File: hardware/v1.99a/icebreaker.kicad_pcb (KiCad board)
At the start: 4 copper layers, 50 x 37 mm, 125 parts, among them J1 USB_C_Receptacle_USB2.0, J14 Jumper, J19 Jumper, J2 Conn_02x05_Odd_Even, J20 Flash, J21 PMOD, J22 PMOD, J23 PMOD, J26 5V AUX, J27 5V AUX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

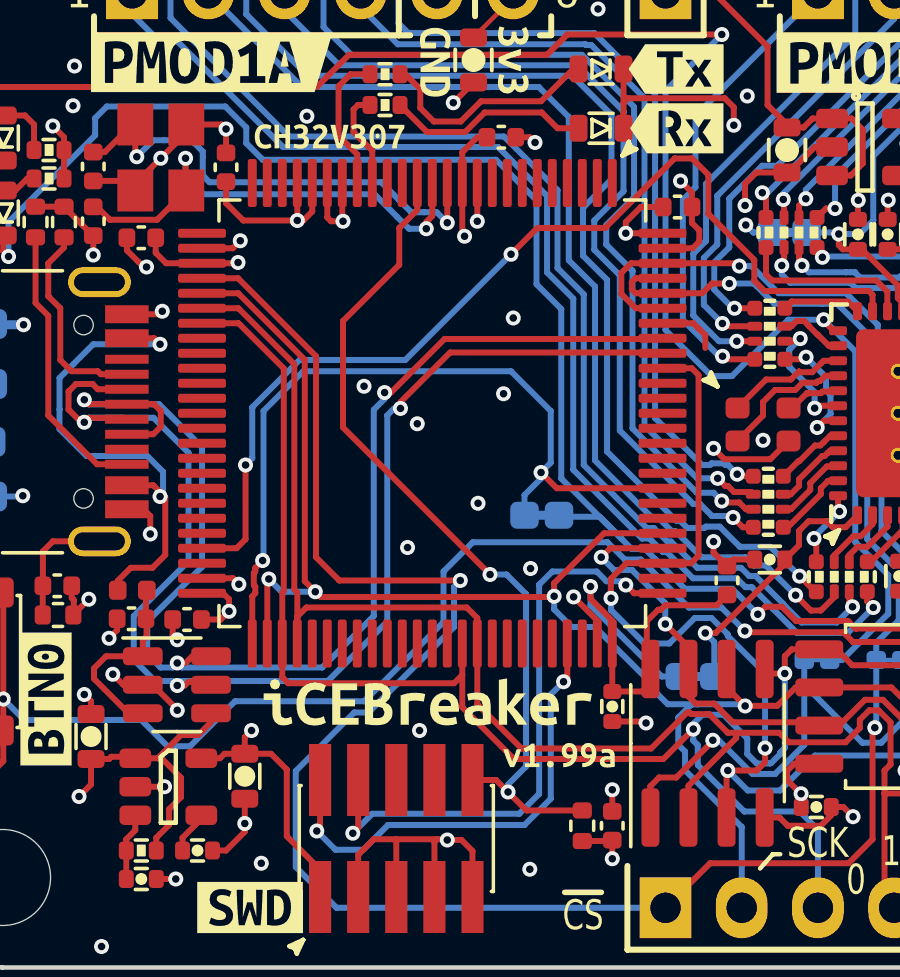
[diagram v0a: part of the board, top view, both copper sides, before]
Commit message: v1.99a: Move FGPA_CLK to MCO pin.
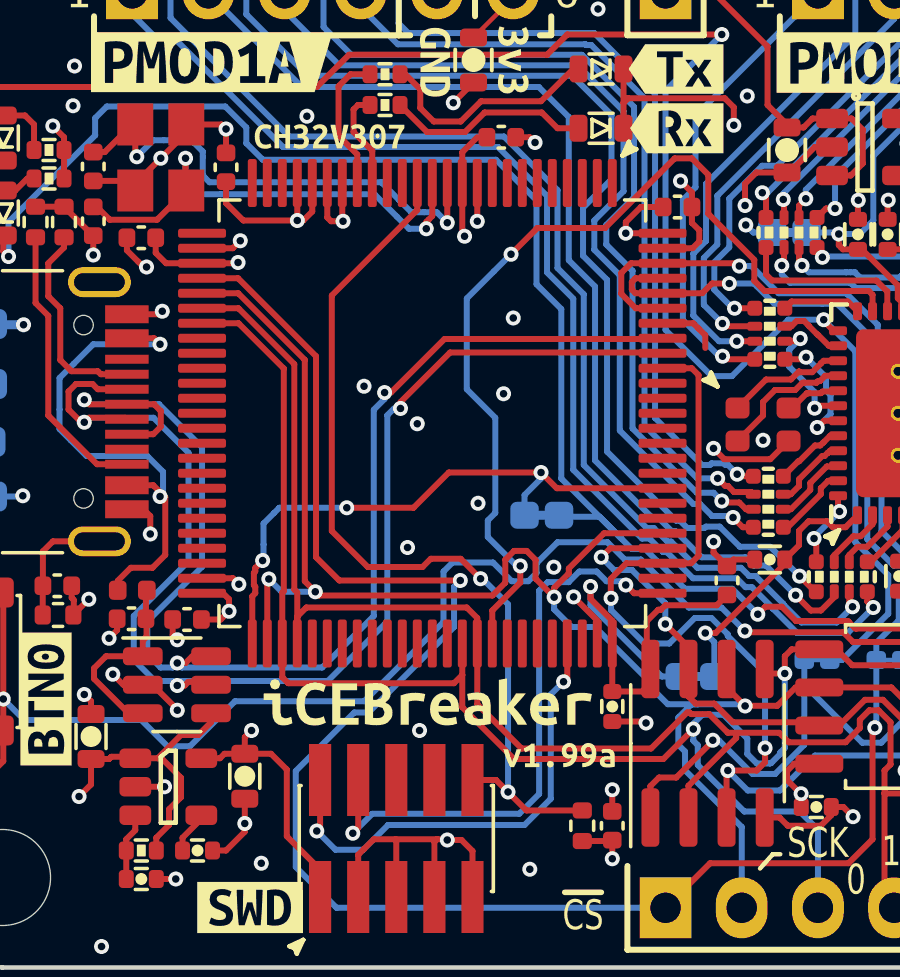
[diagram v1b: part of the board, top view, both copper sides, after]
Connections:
- U4 pad 47: FTDI_CLK -> unconnected-(U4-Pad47)
- U4 pad 67: unconnected-(U4-Pad67) -> FTDI_CLK
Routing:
- net iCE_CS: track 26.7 -> 20.1 mm, vias 2 -> 3
- net iCE_SCK: track 69.7 -> 71.8 mm
- net FTDI_CLK: track 33.8 -> 32.0 mm
- net /usb-if/NRST: track 28.5 -> 30.2 mm
- net /~{BUTTON}: track 51.6 -> 52.4 mm

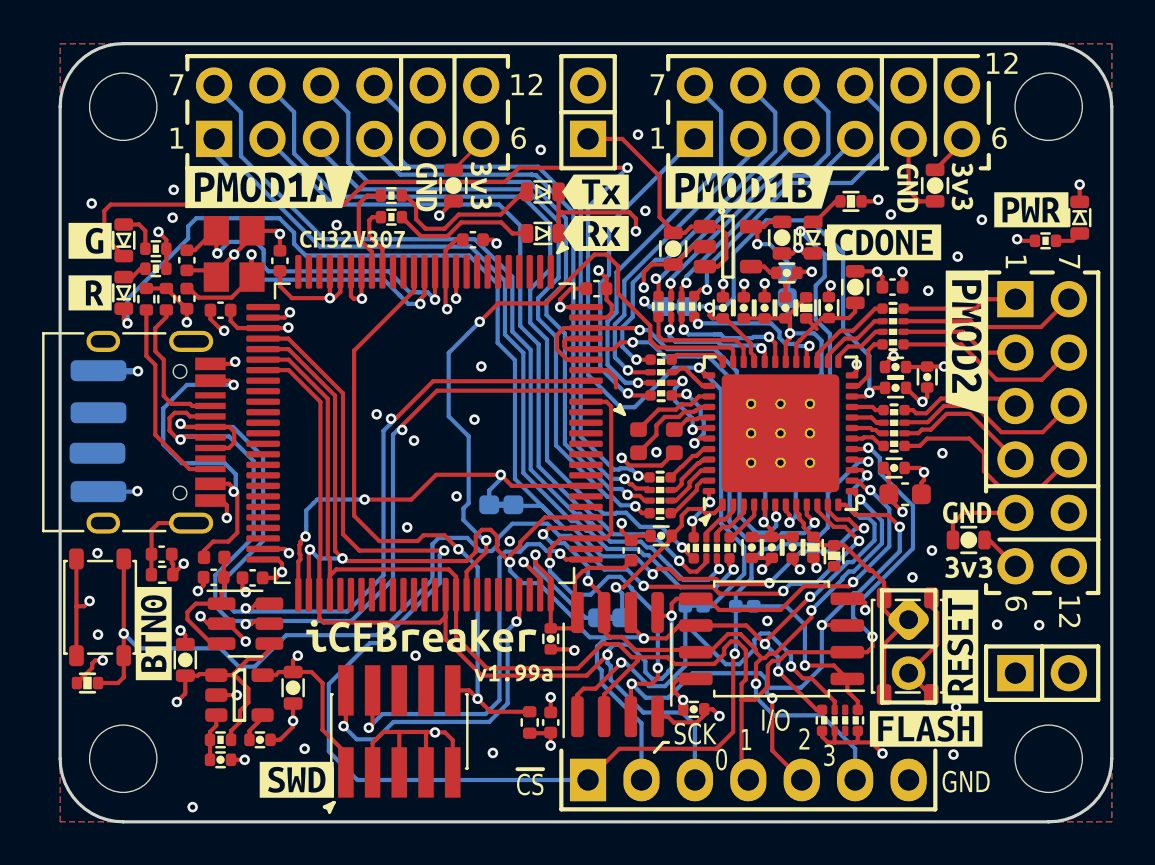
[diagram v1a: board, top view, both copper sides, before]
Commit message: v1.99a: Update
- Rename nets
- Add Debug UART channel to 10P SWD connector
- Add analog mux default on for iCE_CS/FLASH_CS
- Connect DONE/RESET
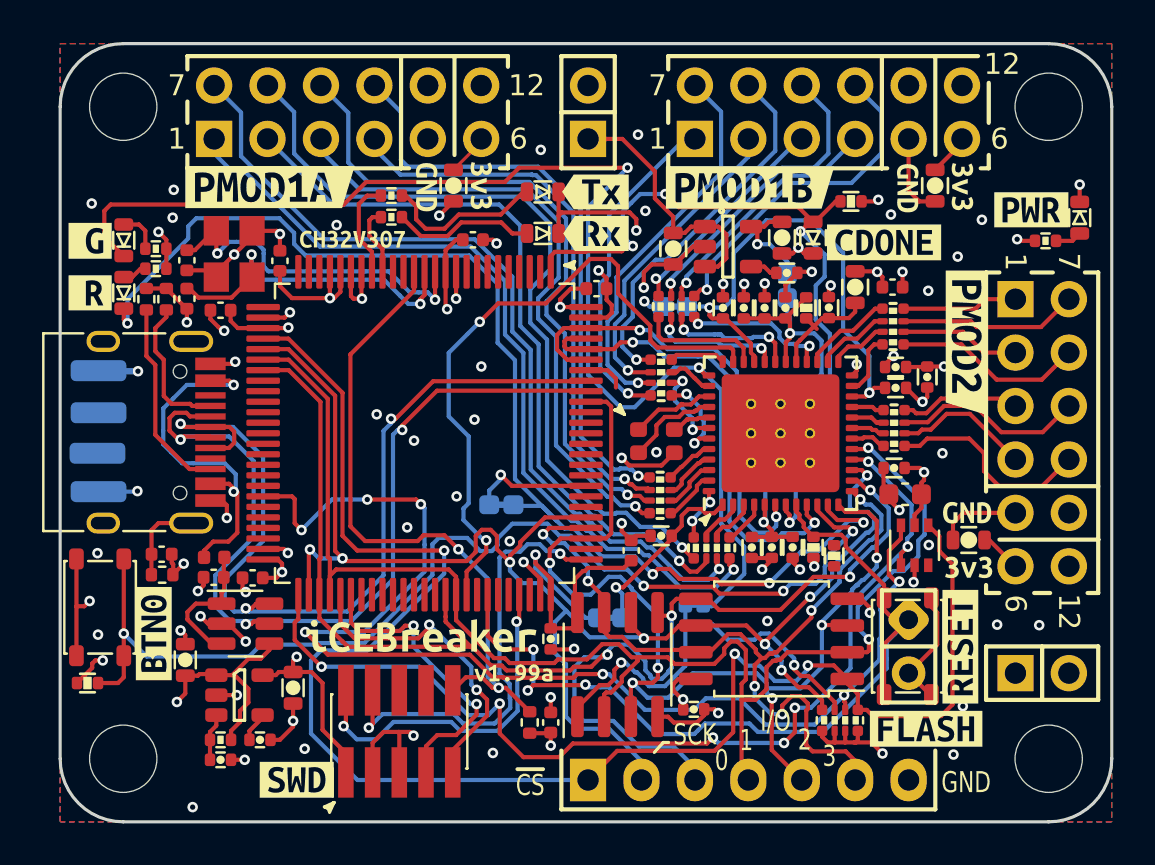
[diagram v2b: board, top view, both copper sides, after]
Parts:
- removed JP2: Flash_CS-SPI_CS, pkl_jumpers:J_NC_0402_15
- added U8: 74LVC1G3157, Package_TO_SOT_SMD:SOT-363_SC-70-6, F.Cu at (70.6, 52.9)
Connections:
- net FLASH_MISO|IO1 renamed FLASH_CIPO|IO1
- net FLASH_MOSI|IO0 renamed FLASH_COPI|IO0
- D3 pad A: /iCE_CDONE -> iCE_CDONE
- J2 pad 7: GND -> /usb-if/DEBUG_RXD
- J2 pad 9: GND -> /usb-if/DEBUG_TXD
- J28 pad 1: /iCE_CRESET -> iCE_CRESET
- J3 pad 2: iCE_CS -> iCE_USER_CS
- R12 pad 2: /iCE_CDONE -> iCE_CDONE
- R19 pad 2: /iCE_CRESET -> iCE_CRESET
- R7 pad 5: (no net) -> +3V3
- R7 pad 6: (no net) -> iCE_CS_SEL
- R7 pad 8: /FLASH_~{CS} -> FLASH_CS
- SW2 pad 1: /iCE_CRESET -> iCE_CRESET
- U4 pad 1: unconnected-(U4-Pad1) -> iCE_CDONE
- U4 pad 44: unconnected-(U4-Pad44) -> iCE_CS_SEL
- U4 pad 55: unconnected-(U4-Pad55) -> /usb-if/DEBUG_TXD
- U4 pad 56: unconnected-(U4-Pad56) -> /usb-if/DEBUG_RXD
- U4 pad 69: unconnected-(U4-Pad69) -> iCE_CRESET
- U4 pad 83: iCE_CS -> iCE_USER_CS
- U6 pad 16: FLASH_CS -> iCE_CS
- U6 pad 35: FTDI_CLK -> FPGA_CLK
- U6 pad 7: /iCE_CDONE -> iCE_CDONE
- U6 pad 8: /iCE_CRESET -> iCE_CRESET
- U7 pad 1: /FLASH_~{CS} -> FLASH_CS
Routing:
- net iCE_CS_SEL: track 0.00 -> 58.8 mm, vias 0 -> 7
- net iCE_CRESET: track 0.00 -> 42.0 mm, vias 0 -> 3
- net iCE_CDONE: track 0.00 -> 36.1 mm, vias 0 -> 4
- net FTDI_CLK: track 32.0 -> 0.00 mm, vias 2 -> 0
- net FPGA_CLK: track 0.00 -> 31.8 mm, vias 0 -> 2
- net iCE_CS: track 20.1 -> 48.6 mm, vias 3 -> 7
- net /iCE_CDONE: track 19.4 -> 0.00 mm, vias 2 -> 0
- net /usb-if/DEBUG_TXD: track 0.00 -> 15.1 mm, vias 0 -> 2
- net /usb-if/DEBUG_RXD: track 0.00 -> 14.5 mm, vias 0 -> 2
- net /iCE_CRESET: track 12.8 -> 0.00 mm
- net FLASH_CS: track 67.3 -> 77.2 mm
- net /FLASH_~{CS}: track 8.69 -> 0.00 mm, vias 1 -> 0
- net iCE_USER_CS: track 0.00 -> 5.92 mm, vias 0 -> 1
- net GND: track 106.0 -> 101.2 mm, vias 79 -> 78
- net FLASH_COPI|IO0: track 64.0 -> 67.5 mm
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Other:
- board text removed: "FLASH CS"

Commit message: Clean up the design.
- Remove R26.
- Connect BOOT0/1 to GND.
- Make schematic a single page.
- Rename labels to OSHWA recommendations.
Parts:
- removed R26: 2k2, pkl_dipol:R_0402
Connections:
- net /usb-if/DEBUG_RXD renamed /DEBUG_RXD
- net /usb-if/DEBUG_TXD renamed /DEBUG_TXD
- net /usb-if/NRST renamed /NRST
- net /usb-if/SHLD renamed /SHLD
- net /usb-if/SWCLK renamed /SWCLK
- net /usb-if/SWDIO renamed /SWDIO
- net /usb-if/USB_N renamed /USB_N
- net /usb-if/USB_P renamed /USB_P
- net /usb-if/VUSB renamed /VUSB
- net FLASH_CIPO|IO1 renamed /SPI_POCI|IO1
- net FLASH_COPI|IO0 renamed /SPI_PICO|IO0
- net FLASH_CS renamed /FLASH_~{CS}
- net FLASH_~{HLD}|~{RST}|IO3 renamed /FLASH_~{HLD}|~{RST}|IO3
- net FLASH_~{WP}|IO2 renamed /FLASH_~{WP}|IO2
- net Rx_TTL renamed /Rx_TTL
- net Tx_TTL renamed /Tx_TTL
- net iCE_CDONE renamed /iCE_CDONE
- net iCE_CS renamed /iCE_~{CS}
- net iCE_CS_SEL renamed /iCE_CS_SEL
- net iCE_SCK renamed /SPI_SCK
- net iCE_USER_CS renamed /iCE_USER_~{CS}
- J28 pad 1: iCE_CRESET -> /iCE_CRESET
- R19 pad 2: iCE_CRESET -> /iCE_CRESET
- SW2 pad 1: iCE_CRESET -> /iCE_CRESET
- U4 pad 37: unconnected-(U4-Pad37) -> GND
- U4 pad 67: FTDI_CLK -> /FPGA_CLK
- U4 pad 69: iCE_CRESET -> /iCE_CRESET
- U4 pad 94: /usb-if/BOOT -> GND
- U6 pad 35: FPGA_CLK -> /FPGA_CLK
- U6 pad 8: iCE_CRESET -> /iCE_CRESET
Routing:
- net iCE_CRESET: track 42.0 -> 0.00 mm, vias 3 -> 0
- net /iCE_CRESET: track 0.00 -> 42.0 mm, vias 0 -> 3
- net FPGA_CLK: track 31.8 -> 0.00 mm, vias 2 -> 0
- net /FPGA_CLK: track 0.00 -> 31.8 mm, vias 0 -> 2
- net /usb-if/BOOT: track 2.02 -> 0.00 mm
